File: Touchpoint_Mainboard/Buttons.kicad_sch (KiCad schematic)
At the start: 9 parts, among them SW1 SW_SPST, SW2 SW_SPST, SW3 SW_SPST

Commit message: Finished assigning footprints and 3d models for both boards
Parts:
- SW3: footprint Button_Switch_THT:SW_PUSH_6mm -> Touchpoint:SW_SPST_EVQP0
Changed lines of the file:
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@@
 			)
 		)
-		(property "Footprint" "Button_Switch_THT:SW_PUSH_6mm"
+		(property "Footprint" "Touchpoint:SW_SPST_EVQP0"
 			(at 88.9 31.75 0)
 			(effects

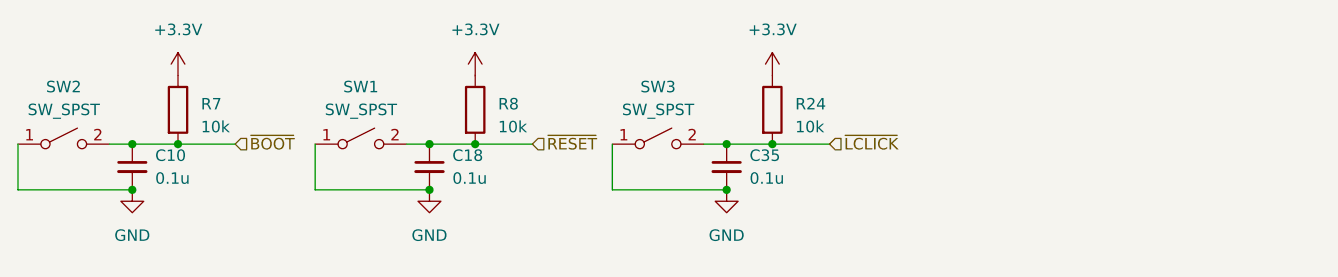
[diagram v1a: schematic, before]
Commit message: Added 3.3V to interface
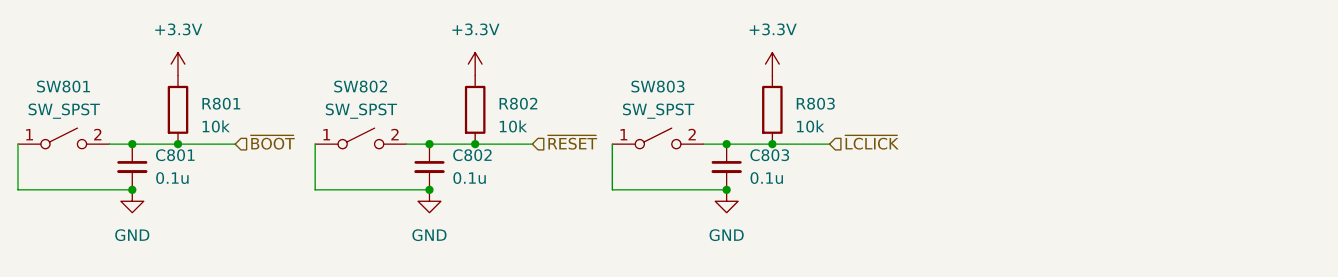
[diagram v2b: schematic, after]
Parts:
- SW803: renamed from SW3; footprint Touchpoint:SW_SPST_EVQP0 -> Connector_Wire:SolderWire-0.1sqmm_1x02_P3.6mm_D0.4mm_OD1mm
- renumbered C10 to C801, C18 to C802, C35 to C803, R7 to R801, R8 to R802, R24 to R803, SW2 to SW801, SW1 to SW802
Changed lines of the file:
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@@
 		(dnp no)
 		(fields_autoplaced yes)
-		(property "Reference" "C18"
+		(property "Reference" "C802"
 			(at 66.04 33.0262 0)
 			(effects
@@
 			(project "Touchpoint_Mainboard"
 				(path "/f37b5f88-420a-4646-85df-8f9851d23e3c/6f657165-8e13-47b4-9d47-bea92f854d29"
-					(reference "C18")
+					(reference "C802")
 					(unit 1)
 				)
@@
 		(dnp no)
 		(fields_autoplaced yes)
-		(property "Reference" "#PWR067"
+		(property "Reference" "#PWR0805"
 			(at 96.52 43.18 0)
 			(effects
@@
 			(project "Touchpoint_Mainboard"
 				(path "/f37b5f88-420a-4646-85df-8f9851d23e3c/6f657165-8e13-47b4-9d47-bea92f854d29"
-					(reference "#PWR067")
+					(reference "#PWR0805")
 					(unit 1)
 				)
@@
 		(dnp no)
 		(fields_autoplaced yes)
-		(property "Reference" "SW3"
+		(property "Reference" "SW803"
 			(at 88.9 25.4 0)
 			(effects
@@
 			)
 		)
-		(property "Footprint" "Touchpoint:SW_SPST_EVQP0"
+		(property "Footprint" "Connector_Wire:SolderWire-0.1sqmm_1x02_P3.6mm_D0.4mm_OD1mm"
 			(at 88.9 31.75 0)
 			(effects
@@
 			(project "Touchpoint_Mainboard"
 				(path "/f37b5f88-420a-4646-85df-8f9851d23e3c/6f657165-8e13-47b4-9d47-bea92f854d29"
-					(reference "SW3")
+					(reference "SW803")
 					(unit 1)
 				)
@@
 		(dnp no)
 		(fields_autoplaced yes)
-		(property "Reference" "R7"
+		(property "Reference" "R801"
 			(at 38.1 27.305 0)
 			(effects
@@
 			(project "Touchpoint_Mainboard"
 				(path "/f37b5f88-420a-4646-85df-8f9851d23e3c/6f657165-8e13-47b4-9d47-bea92f854d29"
-					(reference "R7")
+					(reference "R801")
 					(unit 1)
 				)
@@
 		(dnp no)
 		(fields_autoplaced yes)
-		(property "Reference" "C35"
+		(property "Reference" "C803"
 			(at 99.06 33.0262 0)
 			(effects
@@
 			(project "Touchpoint_Mainboard"
 				(path "/f37b5f88-420a-4646-85df-8f9851d23e3c/6f657165-8e13-47b4-9d47-bea92f854d29"
-					(reference "C35")
+					(reference "C803")
 					(unit 1)
 				)
@@
 		(dnp no)
 		(fields_autoplaced yes)
-		(property "Reference" "C10"
+		(property "Reference" "C801"
 			(at 33.02 33.0262 0)
 			(effects
@@
 			(project "Touchpoint_Mainboard"
 				(path "/f37b5f88-420a-4646-85df-8f9851d23e3c/6f657165-8e13-47b4-9d47-bea92f854d29"
-					(reference "C10")
+					(reference "C801")
 					(unit 1)
 				)
@@
 		(dnp no)
 		(fields_autoplaced yes)
-		(property "Reference" "R8"
+		(property "Reference" "R802"
 			(at 71.12 27.305 0)
 			(effects
@@
 			(project "Touchpoint_Mainboard"
 				(path "/f37b5f88-420a-4646-85df-8f9851d23e3c/6f657165-8e13-47b4-9d47-bea92f854d29"
-					(reference "R8")
+					(reference "R802")
 					(unit 1)
 				)
@@
 		(dnp no)
 		(fields_autoplaced yes)
-		(property "Reference" "SW1"
+		(property "Reference" "SW802"
 			(at 55.88 25.4 0)
 			(effects
@@
 			(project "Touchpoint_Mainboard"
 				(path "/f37b5f88-420a-4646-85df-8f9851d23e3c/6f657165-8e13-47b4-9d47-bea92f854d29"
-					(reference "SW1")
+					(reference "SW802")
 					(unit 1)
 				)
@@
 		(dnp no)
 		(fields_autoplaced yes)
-		(property "Reference" "R24"
+		(property "Reference" "R803"
 			(at 104.14 27.305 0)
 			(effects
@@
 			(project "Touchpoint_Mainboard"
 				(path "/f37b5f88-420a-4646-85df-8f9851d23e3c/6f657165-8e13-47b4-9d47-bea92f854d29"
-					(reference "R24")
+					(reference "R803")
 					(unit 1)
 				)
@@
 		(dnp no)
 		(fields_autoplaced yes)
-		(property "Reference" "#PWR019"
+		(property "Reference" "#PWR0802"
 			(at 35.56 27.94 0)
 			(effects
@@
 			(project "Touchpoint_Mainboard"
 				(path "/f37b5f88-420a-4646-85df-8f9851d23e3c/6f657165-8e13-47b4-9d47-bea92f854d29"
-					(reference "#PWR019")
+					(reference "#PWR0802")
 					(unit 1)
 				)
@@
 		(dnp no)
 		(fields_autoplaced yes)
-		(property "Reference" "#PWR018"
+		(property "Reference" "#PWR0801"
 			(at 30.48 43.18 0)
 			(effects
@@
 			(project "Touchpoint_Mainboard"
 				(path "/f37b5f88-420a-4646-85df-8f9851d23e3c/6f657165-8e13-47b4-9d47-bea92f854d29"
-					(reference "#PWR018")
+					(reference "#PWR0801")
 					(unit 1)
 				)
@@
 		(dnp no)
 		(fields_autoplaced yes)
-		(property "Reference" "#PWR068"
+		(property "Reference" "#PWR0806"
 			(at 101.6 27.94 0)
 			(effects
@@
 			(project "Touchpoint_Mainboard"
 				(path "/f37b5f88-420a-4646-85df-8f9851d23e3c/6f657165-8e13-47b4-9d47-bea92f854d29"
-					(reference "#PWR068")
+					(reference "#PWR0806")
 					(unit 1)
 				)
@@
 		(dnp no)
 		(fields_autoplaced yes)
-		(property "Reference" "#PWR012"
+		(property "Reference" "#PWR0803"
 			(at 63.5 43.18 0)
 			(effects
@@
 			(project "Touchpoint_Mainboard"
 				(path "/f37b5f88-420a-4646-85df-8f9851d23e3c/6f657165-8e13-47b4-9d47-bea92f854d29"
-					(reference "#PWR012")
+					(reference "#PWR0803")
 					(unit 1)
 				)
@@
 		(dnp no)
 		(fields_autoplaced yes)
-		(property "Reference" "#PWR025"
+		(property "Reference" "#PWR0804"
 			(at 68.58 27.94 0)
 			(effects
@@
 			(project "Touchpoint_Mainboard"
 				(path "/f37b5f88-420a-4646-85df-8f9851d23e3c/6f657165-8e13-47b4-9d47-bea92f854d29"
-					(reference "#PWR025")
+					(reference "#PWR0804")
 					(unit 1)
 				)
@@
 		(dnp no)
 		(fields_autoplaced yes)
-		(property "Reference" "SW2"
+		(property "Reference" "SW801"
 			(at 22.86 25.4 0)
 			(effects
@@
 			(project "Touchpoint_Mainboard"
 				(path "/f37b5f88-420a-4646-85df-8f9851d23e3c/6f657165-8e13-47b4-9d47-bea92f854d29"
-					(reference "SW2")
-					(unit 1)
-				)
+					(reference "SW801")
+					(unit 1)
+				)

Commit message: Final manufacturing adjustments
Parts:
- added C804, C805, C806: 0.1u, Capacitor_SMD:C_0402_1005Metric, symbol Device:C_Small
- added R804, R805, R806: 10k, Resistor_SMD:R_0402_1005Metric, symbol Device:R
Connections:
- net +3.3V: now also R804.1, R805.1, R806.1
- net GND: now also C804.2, C805.2, C806.2
- new net RCLICK: C804.1, R804.2
- new net SCROLLA: C805.1, R805.2
- new net SCROLLB: C806.1, R806.2
